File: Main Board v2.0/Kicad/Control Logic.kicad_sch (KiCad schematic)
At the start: 25 parts, among them J3 JTAG, J4 +3V3 Supply, J5 Conn_02x14_Counter_Clockwise, U7 XC95288XL-TQ144, U8 AP1117-33

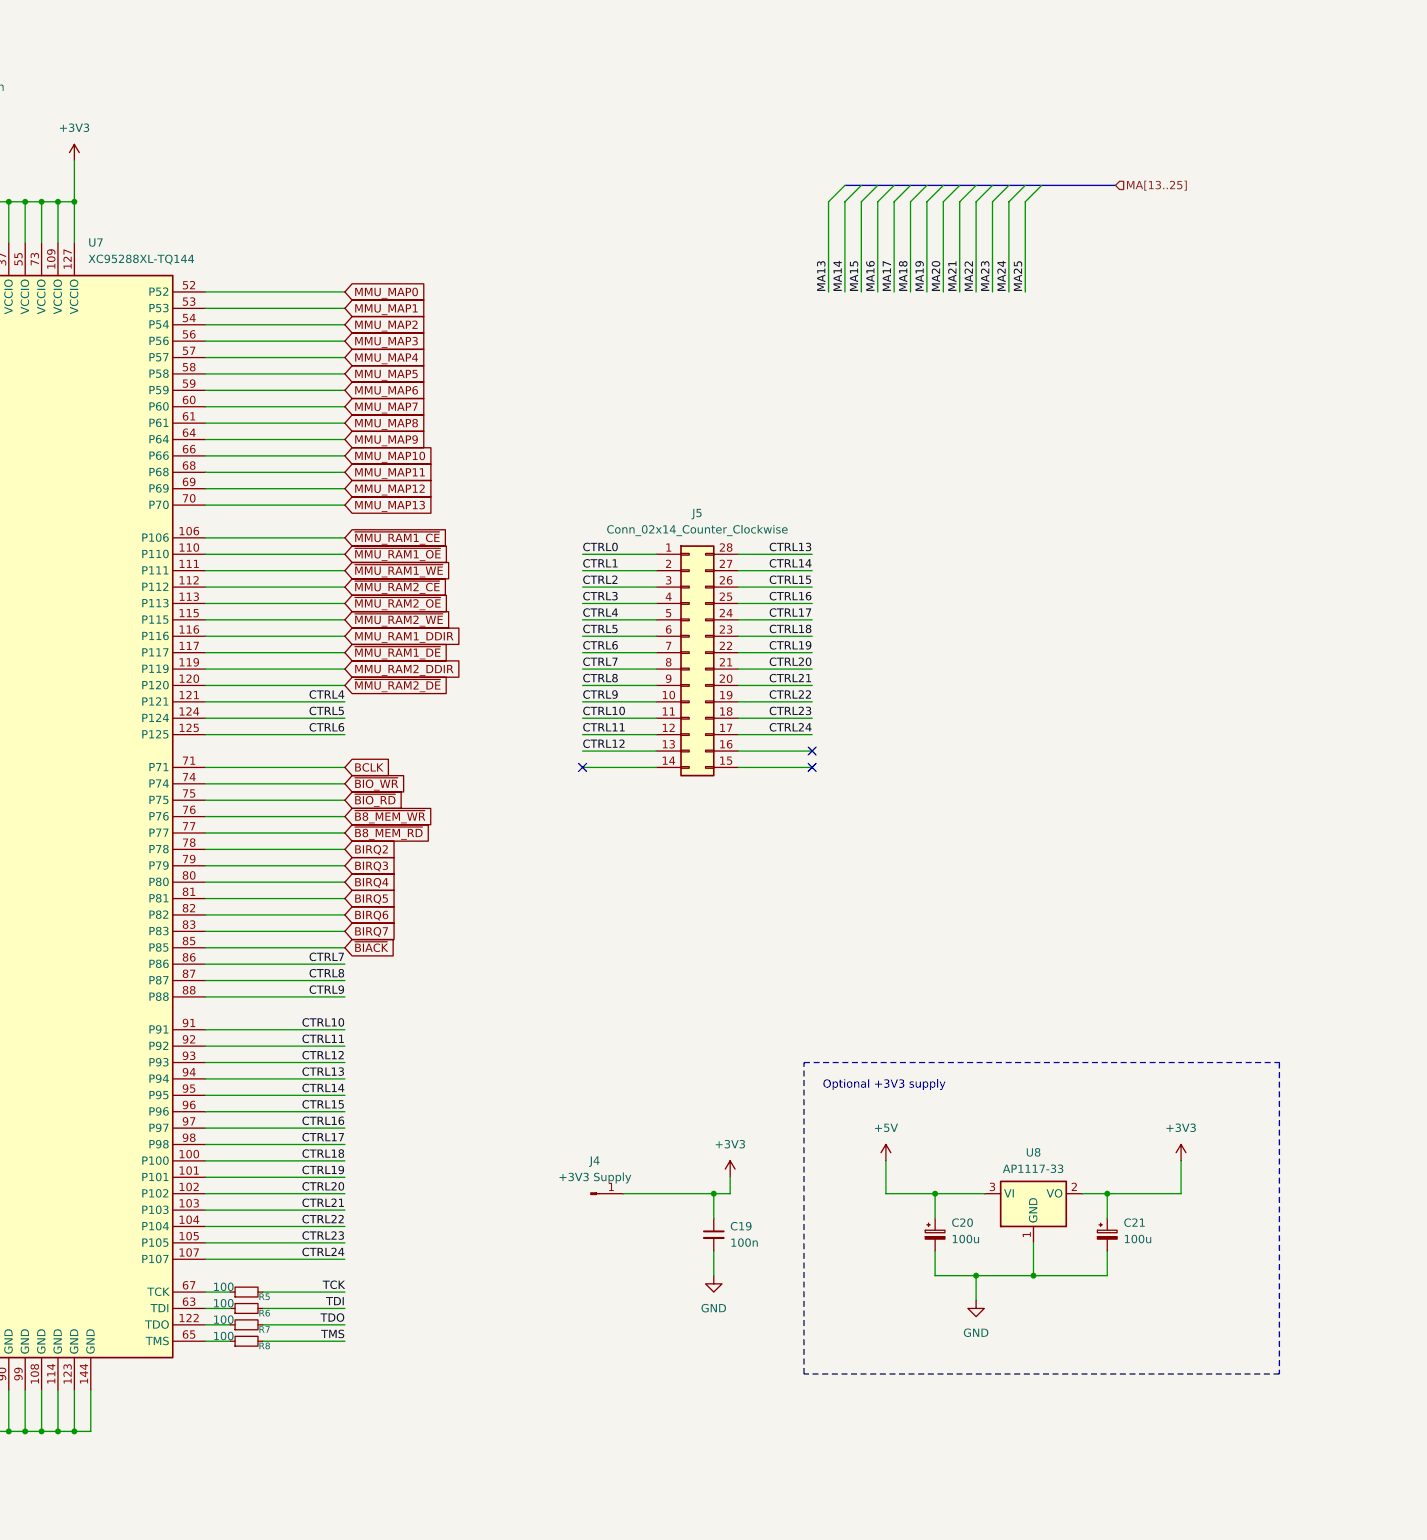
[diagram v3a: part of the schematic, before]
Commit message: schematic update
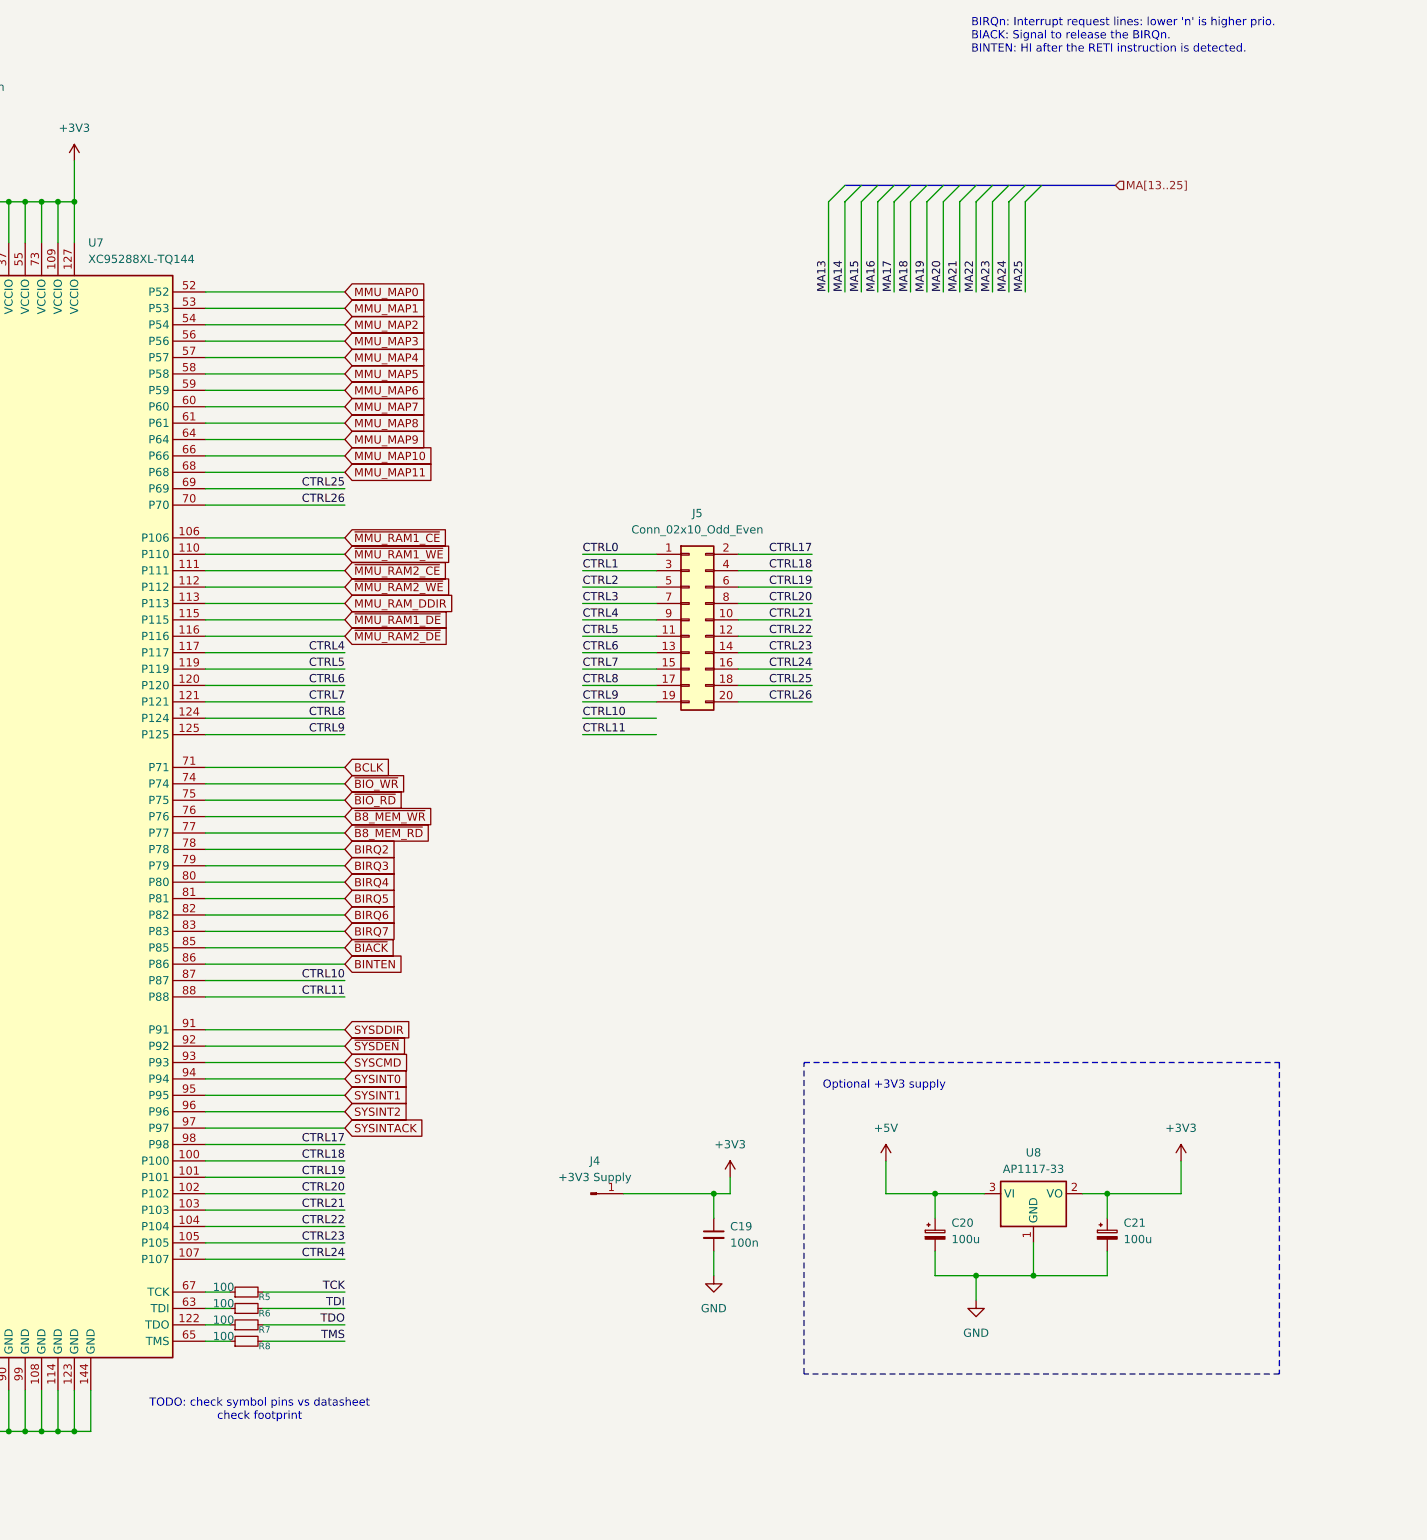
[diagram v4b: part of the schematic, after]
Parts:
- removed J5: Conn_02x14_Counter_Clockwise, Connector_PinSocket_2.54mm:PinSocket_2x14_P2.54mm_Vertical, symbol Connector_Generic:Conn_02x14_Counter_Clockwise
- added J5: Conn_02x10_Odd_Even, Connector_PinSocket_2.54mm:PinSocket_2x10_P2.54mm_Vertical, symbol Connector_Generic:Conn_02x10_Odd_Even
- C20, C21: footprint Capacitor_THT:CP_Radial_D10.0mm_P5.00mm -> Capacitor_THT:CP_Radial_D8.0mm_P3.80mm
- J3: footprint Connector_PinHeader_2.54mm:PinHeader_2x07_P2.54mm_Vertical -> Connector_IDC:IDC-Header_2x07_P2.54mm_Vertical
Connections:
- net MMU_RAM1_DDIR is gone; now on net ~{MMU_RAM2_DE}: U7.116 (P116)
- net MMU_RAM2_DDIR is gone; now on net CTRL5: U7.119 (P119)
- net ~{MMU_RAM1_OE} is gone; now on net ~{MMU_RAM1_WE}: U7.110 (P110)
- net CTRL0: now also J5.1 (Pin_1)
- net CTRL1: now also J5.3 (Pin_3)
- net CTRL10: now also U7.87 (P87); no longer U7.91 (P91)
- net CTRL11: now also U7.88 (P88); no longer U7.92 (P92)
- net CTRL17: now also J5.2 (Pin_2)
- net CTRL18: now also J5.4 (Pin_4)
- net CTRL19: now also J5.6 (Pin_6)
- net CTRL2: now also J5.5 (Pin_5)
- net CTRL20: now also J5.8 (Pin_8)
- net CTRL21: now also J5.10 (Pin_10)
- net CTRL22: now also J5.12 (Pin_12)
- net CTRL23: now also J5.14 (Pin_14)
- net CTRL24: now also J5.16 (Pin_16)
- net CTRL3: now also J5.7 (Pin_7)
- net CTRL4: now also U7.117 (P117), J5.9 (Pin_9); no longer U7.121 (P121)
- net CTRL5: now also J5.11 (Pin_11); no longer U7.124 (P124)
- net CTRL6: now also U7.120 (P120), J5.13 (Pin_13); no longer U7.125 (P125)
- net CTRL7: now also U7.121 (P121), J5.15 (Pin_15); no longer U7.86 (P86)
- net CTRL8: now also U7.124 (P124), J5.17 (Pin_17); no longer U7.87 (P87)
- net CTRL9: now also U7.125 (P125), J5.19 (Pin_19); no longer U7.88 (P88)
- net ~{MMU_RAM1_DE}: now also U7.115 (P115); no longer U7.117 (P117)
- net ~{MMU_RAM1_WE}: no longer U7.111 (P111)
- net ~{MMU_RAM2_CE}: now also U7.111 (P111); no longer U7.112 (P112)
- net ~{MMU_RAM2_DE}: no longer U7.120 (P120)
- net ~{MMU_RAM2_WE}: now also U7.112 (P112); no longer U7.115 (P115)
- net CTRL12 renamed SYSCMD
- net CTRL13 renamed SYSINT0
- net CTRL14 renamed SYSINT1
- net CTRL15 renamed SYSINT2
- net CTRL16 renamed SYSINTACK
- net MMU_MAP12 renamed CTRL25
- net CTRL25: now also J5.18 (Pin_18)
- net MMU_MAP13 renamed CTRL26
- net CTRL26: now also J5.20 (Pin_20)
- net ~{MMU_RAM2_OE} renamed MMU_RAM_DDIR
- new net BINTEN: U7.86 (P86)
- new net SYSDDIR: U7.91 (P91)
- new net ~{SYSDEN}: U7.92 (P92)
- no-connect marks 5 -> 2
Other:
- note added: "BIRQn: Interrupt request lines: lower 'n' is higher prio. BIACK: Signal to release the BIRQn. BINTEN: HI after the RETI instruction is detected."
- note added: "TODO: check symbol pins vs datasheet check footprint"

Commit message: schematic updates
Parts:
- removed J5: Conn_02x10_Odd_Even, Connector_PinSocket_2.54mm:PinSocket_2x10_P2.54mm_Vertical, symbol Connector_Generic:Conn_02x10_Odd_Even
- renumbered C12 to C10, C13 to C11, C14 to C12, C15 to C13, C16 to C14, C17 to C15, C18 to C16, C19 to C17, C20 to C18, C21 to C19, C9 to C7, C10 to C8, C11 to C9, J4 to J2, R5 to R28, R6 to R29, R7 to R30, R8 to R31, R2 to R32, R3 to R33, R4 to R34
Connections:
- net CTRL10 is gone; now on net ~{BIACK}: U7.87 (P87)
- net CTRL11 is gone; now on net BINTEN: U7.88 (P88)
- net BINTEN: no longer U7.86 (P86)
- net BIRQ2: now also U7.80 (P80); no longer U7.78 (P78)
- net BIRQ3: now also U7.81 (P81); no longer U7.79 (P79)
- net BIRQ4: now also U7.82 (P82); no longer U7.80 (P80)
- net BIRQ5: now also U7.83 (P83); no longer U7.81 (P81)
- net BIRQ6: now also U7.85 (P85); no longer U7.82 (P82)
- net BIRQ7: now also U7.86 (P86); no longer U7.83 (P83)
- net ~{BIACK}: no longer U7.85 (P85)
- net CTRL0 renamed BC11
- net CTRL1 renamed BC12
- net CTRL17 renamed BINTACK0
- net CTRL18 renamed BINTACK1
- net CTRL19 renamed BINTACK2
- net CTRL2 renamed BC13
- net CTRL20 renamed BINTACK3
- net CTRL21 renamed BINTACK4
- net CTRL22 renamed BINTACK5
- net CTRL23 renamed BINTACK6
- net CTRL24 renamed BINTACK7
- net CTRL25 renamed BC1
- net CTRL26 renamed BC6
- net CTRL3 renamed BC14
- net CTRL4 renamed BA1
- net CTRL5 renamed BB4
- net CTRL6 renamed BC15
- net CTRL7 renamed BC16
- net CTRL8 renamed BC17
- net CTRL9 renamed BC18
- new net BIRQ0: U7.78 (P78)
- new net BIRQ1: U7.79 (P79)
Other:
- note removed: "TODO: check symbol pins vs datasheet check footprint"

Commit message: board update
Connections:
- net BC6 is gone; now on net ~{CPU_RST}: U7.70 (P70)
- net MA25 is gone; now on net ~{CPU_INT}: U7.131 (P131)
- net MMU_MAP11 is gone; now on net D7: U7.68 (P68)
- net A0: now also U7.26 (P26); no longer U7.16 (P16)
- net A1: now also U7.27 (P27); no longer U7.17 (P17)
- net A10: now also U7.43 (P43); no longer U7.27 (P27)
- net A11: now also U7.44 (P44); no longer U7.28 (P28)
- net A12: now also U7.9 (P9); no longer U7.30 (I/O/GCK1)
- net A13: now also U7.10 (P10); no longer U7.31 (P31)
- net A14: now also U7.11 (P11); no longer U7.35 (P35)
- net A15: now also U7.12 (P12); no longer U7.2 (I/O/GTS3)
- net A2: now also U7.28 (P28); no longer U7.19 (P19)
- net A3: now also U7.30 (I/O/GCK1); no longer U7.20 (P20)
- net A4: now also U7.31 (P31); no longer U7.21 (P21)
- net A5: now also U7.35 (P35); no longer U7.22 (P22)
- net A6: now also U7.38 (I/O/GCK3); no longer U7.23 (P23)
- net A7: now also U7.39 (P39); no longer U7.24 (P24)
- net A8: now also U7.40 (P40); no longer U7.25 (P25)
- net A9: now also U7.41 (P41); no longer U7.26 (P26)
- net BA1: now also U7.69 (P69); no longer U7.117 (P117)
- net BB4: now also U7.71 (P71); no longer U7.119 (P119)
- net BC1: now also U7.24 (P24); no longer U7.69 (P69)
- net BC11: now also U7.132 (P132); no longer U7.137 (P137)
- net BC12: now also U7.133 (P133); no longer U7.138 (P138)
- net BC13: now also U7.134 (P134); no longer U7.139 (P139)
- net BC14: now also U7.135 (P135); no longer U7.140 (P140)
- net BC15: now also U7.136 (P136); no longer U7.120 (P120)
- net BC16: now also U7.137 (P137); no longer U7.121 (P121)
- net BC17: now also U7.138 (P138); no longer U7.124 (P124)
- net BC18: now also U7.139 (P139); no longer U7.125 (P125)
- net BCLK: now also U7.83 (P83); no longer U7.71 (P71)
- net BINTACK0: now also U7.16 (P16); no longer U7.98 (P98)
- net BINTACK1: now also U7.17 (P17); no longer U7.100 (P100)
- net BINTACK2: now also U7.2 (I/O/GTS3); no longer U7.101 (P101)
- net BINTACK3: now also U7.3 (I/O/GTS4); no longer U7.102 (P102)
- net BINTACK4: now also U7.4 (P4); no longer U7.103 (P103)
- net BINTACK5: now also U7.5 (I/O/GTS1); no longer U7.104 (P104)
- net BINTACK6: now also U7.6 (I/O/GTS2); no longer U7.105 (P105)
- net BINTACK7: now also U7.7 (P7); no longer U7.107 (P107)
- net BINTEN: now also U7.79 (P79); no longer U7.88 (P88)
- net BIRQ0: now also U7.32 (I/O/GCK2); no longer U7.78 (P78)
- net BIRQ1: now also U7.33 (P33); no longer U7.79 (P79)
- net BIRQ2: now also U7.34 (P34); no longer U7.80 (P80)
- net BIRQ3: now also U7.140 (P140); no longer U7.81 (P81)
- net BIRQ4: now also U7.88 (P88); no longer U7.82 (P82)
- net BIRQ5: now also U7.87 (P87); no longer U7.83 (P83)
- net BIRQ6: now also U7.86 (P86); no longer U7.85 (P85)
- net BIRQ7: now also U7.85 (P85); no longer U7.86 (P86)
- net CLK20: now also U7.13 (P13); no longer U7.32 (I/O/GCK2)
- net D0: now also U7.57 (P57); no longer U7.3 (I/O/GTS4)
- net D1: now also U7.58 (P58); no longer U7.4 (P4)
- net D2: now also U7.59 (P59); no longer U7.5 (I/O/GTS1)
- net D3: now also U7.60 (P60); no longer U7.6 (I/O/GTS2)
- net D4: now also U7.61 (P61); no longer U7.7 (P7)
- net D5: now also U7.64 (P64); no longer U7.9 (P9)
- net D6: now also U7.66 (P66); no longer U7.10 (P10)
- net D7: no longer U7.11 (P11)
- net MA13: now also U7.46 (P46); no longer U7.44 (P44)
- net MA14: now also U7.48 (P48); no longer U7.45 (P45)
- net MA15: now also U7.49 (P49); no longer U7.46 (P46)
- net MA16: now also U7.50 (P50); no longer U7.48 (P48)
- net MA17: now also U7.51 (P51); no longer U7.49 (P49)
- net MA18: now also U7.52 (P52); no longer U7.50 (P50)
- net MA19: now also U7.53 (P53); no longer U7.51 (P51)
- net MA20: now also U7.19 (P19); no longer U7.118 (P118)
- net MA21: now also U7.20 (P20); no longer U7.126 (P126)
- net MA22: now also U7.21 (P21); no longer U7.128 (P128)
- net MA23: now also U7.22 (P22); no longer U7.129 (P129)
- net MA24: now also U7.23 (P23); no longer U7.130 (P130)
- net MMU_MAP0: now also U7.95 (P95); no longer U7.52 (P52)
- net MMU_MAP1: now also U7.96 (P96); no longer U7.53 (P53)
- net MMU_MAP10: now also U7.107 (P107); no longer U7.66 (P66)
- net MMU_MAP2: now also U7.97 (P97); no longer U7.54 (P54)
- net MMU_MAP3: now also U7.98 (P98); no longer U7.56 (P56)
- net MMU_MAP4: now also U7.100 (P100); no longer U7.57 (P57)
- net MMU_MAP5: now also U7.101 (P101); no longer U7.58 (P58)
- net MMU_MAP6: now also U7.102 (P102); no longer U7.59 (P59)
- net MMU_MAP7: now also U7.103 (P103); no longer U7.60 (P60)
- net MMU_MAP8: now also U7.104 (P104); no longer U7.61 (P61)
- net MMU_MAP9: now also U7.105 (P105); no longer U7.64 (P64)
- net MMU_MP_EXE: now also U7.115 (P115); no longer U7.134 (P134)
- net MMU_MP_RD: now also U7.112 (P112); no longer U7.132 (P132)
- net MMU_MP_WR: now also U7.113 (P113); no longer U7.133 (P133)
- net MMU_RAM_DDIR: now also U7.92 (P92); no longer U7.113 (P113)
- net SYSCMD: now also U7.124 (P124); no longer U7.93 (P93)
- net SYSDDIR: now also U7.120 (P120); no longer U7.91 (P91)
- net SYSINT0: now also U7.126 (P126); no longer U7.94 (P94)
- net SYSINT1: now also U7.128 (P128); no longer U7.95 (P95)
- net SYSINT2: now also U7.129 (P129); no longer U7.96 (P96)
- net SYSINTACK: now also U7.125 (P125); no longer U7.97 (P97)
- net ~{B8_MEM_RD}: now also U7.75 (P75); no longer U7.77 (P77)
- net ~{B8_MEM_WR}: now also U7.74 (P74); no longer U7.76 (P76)
- net ~{BIACK}: now also U7.78 (P78); no longer U7.87 (P87)
- net ~{BIO_RD}: now also U7.77 (P77); no longer U7.75 (P75)
- net ~{BIO_WR}: now also U7.76 (P76); no longer U7.74 (P74)
- net ~{CPU_BUSACK}: now also U7.81 (P81); no longer U7.43 (P43)
- net ~{CPU_BUSRQ}: now also U7.80 (P80); no longer U7.41 (P41)
- net ~{CPU_HALT}: now also U7.119 (P119); no longer U7.33 (P33)
- net ~{CPU_INT}: no longer U7.14 (P14)
- net ~{CPU_IORQ}: now also U7.14 (P14); no longer U7.40 (P40)
- net ~{CPU_M1}: now also U7.54 (P54); no longer U7.15 (P15)
- net ~{CPU_MREQ}: now also U7.15 (P15); no longer U7.39 (P39)
- net ~{CPU_NMI}: now also U7.130 (P130); no longer U7.13 (P13)
- net ~{CPU_RD}: now also U7.142 (P142); no longer U7.34 (P34)
- net ~{CPU_RFSH}: now also U7.82 (P82); no longer U7.142 (P142)
- net ~{CPU_RST}: no longer U7.12 (P12)
- net ~{CPU_WAIT}: now also U7.56 (P56); no longer U7.143 (I/O/GSR)
- net ~{CPU_WR}: now also U7.143 (I/O/GSR); no longer U7.38 (I/O/GCK3)
- net ~{MMU_RAM1_CE}: now also U7.110 (P110); no longer U7.106 (P106)
- net ~{MMU_RAM1_DE}: now also U7.93 (P93); no longer U7.115 (P115)
- net ~{MMU_RAM1_WE}: now also U7.111 (P111); no longer U7.110 (P110)
- net ~{MMU_RAM2_CE}: now also U7.106 (P106); no longer U7.111 (P111)
- net ~{MMU_RAM2_DE}: now also U7.94 (P94); no longer U7.116 (P116)
- net ~{MMU_RAM2_WE}: now also U7.91 (P91); no longer U7.112 (P112)
- net ~{RAM_CE}: now also U7.117 (P117); no longer U7.136 (P136)
- net ~{ROM_CE}: now also U7.116 (P116); no longer U7.135 (P135)
- net ~{SYSDEN}: now also U7.121 (P121); no longer U7.92 (P92)
- new net BC2: U7.25 (P25)
- new net BC3: U7.118 (P118)
- new net MA12: U7.45 (P45)

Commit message: board update
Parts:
- removed R28, R29, R30, R31: 100, Resistor_SMD:R_0603_1608Metric_Pad0.98x0.95mm_HandSolder, symbol Device:R_Small
- C10, C11, C12, C13, C14, C15, C16, C17, C7, C8, C9, R32, R33, R34: KiLib_Generator (none) -> SMD_2terminal_chip_molded
- C18, C19: KiLib_Generator (none) -> capacitor/THT/other
- J2, J3: KiLib_Generator (none) -> connector/pin_header_socket
- U7: KiLib_Generator (none) -> package/gullwing
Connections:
- net BA1 is gone; now on net ~{CPU_WAIT}: U7.69 (P69)
- net BB4 is gone; now on net ~{CPU_RST}: U7.71 (P71)
- net A0: now also U7.28 (P28); no longer U7.26 (P26)
- net A1: now also U7.31 (P31); no longer U7.27 (P27)
- net A12: now also U7.136 (P136); no longer U7.9 (P9)
- net A13: now also U7.137 (P137); no longer U7.10 (P10)
- net A14: now also U7.138 (P138); no longer U7.11 (P11)
- net A15: now also U7.139 (P139); no longer U7.12 (P12)
- net A2: now also U7.32 (I/O/GCK2); no longer U7.28 (P28)
- net A3: now also U7.33 (P33); no longer U7.30 (I/O/GCK1)
- net A4: now also U7.34 (P34); no longer U7.31 (P31)
- net BC1: now also U7.27 (P27); no longer U7.24 (P24)
- net BC11: now also U7.16 (P16); no longer U7.132 (P132)
- net BC12: now also U7.15 (P15); no longer U7.133 (P133)
- net BC13: now also U7.14 (P14); no longer U7.134 (P134)
- net BC14: now also U7.13 (P13); no longer U7.135 (P135)
- net BC15: now also U7.12 (P12); no longer U7.136 (P136)
- net BC16: now also U7.11 (P11); no longer U7.137 (P137)
- net BC17: now also U7.10 (P10); no longer U7.138 (P138)
- net BC18: now also U7.9 (P9); no longer U7.139 (P139)
- net BC2: now also U7.26 (P26); no longer U7.25 (P25)
- net BC3: now also U7.25 (P25); no longer U7.118 (P118)
- net BINTACK0: now also U7.118 (P118); no longer U7.16 (P16)
- net BINTACK1: now also U7.132 (P132); no longer U7.17 (P17)
- net BINTACK2: now also U7.85 (P85); no longer U7.2 (I/O/GTS3)
- net BINTACK3: now also U7.86 (P86); no longer U7.3 (I/O/GTS4)
- net BINTACK4: now also U7.87 (P87); no longer U7.4 (P4)
- net BINTACK5: now also U7.7 (P7); no longer U7.5 (I/O/GTS1)
- net BINTACK6: now also U7.5 (I/O/GTS1); no longer U7.6 (I/O/GTS2)
- net BINTACK7: now also U7.3 (I/O/GTS4); no longer U7.7 (P7)
- net BIRQ0: now also U7.133 (P133); no longer U7.32 (I/O/GCK2)
- net BIRQ1: now also U7.134 (P134); no longer U7.33 (P33)
- net BIRQ2: now also U7.135 (P135); no longer U7.34 (P34)
- net BIRQ5: now also U7.6 (I/O/GTS2); no longer U7.87 (P87)
- net BIRQ6: now also U7.4 (P4); no longer U7.86 (P86)
- net BIRQ7: now also U7.2 (I/O/GTS3); no longer U7.85 (P85)
- net CLK20: now also U7.30 (I/O/GCK1); no longer U7.13 (P13)
- net MA20: now also U7.54 (P54); no longer U7.19 (P19)
- net MA21: now also U7.56 (P56); no longer U7.20 (P20)
- net MA22: now also U7.20 (P20); no longer U7.21 (P21)
- net MA23: now also U7.21 (P21); no longer U7.22 (P22)
- net MA24: now also U7.22 (P22); no longer U7.23 (P23)
- net TCK: now also U7.67 (TCK)
- net TDI: now also U7.63 (TDI)
- net TDO: now also U7.122 (TDO)
- net TMS: now also U7.65 (TMS)
- net ~{CPU_IORQ}: now also U7.142 (P142); no longer U7.14 (P14)
- net ~{CPU_M1}: now also U7.70 (P70); no longer U7.54 (P54)
- net ~{CPU_MREQ}: now also U7.143 (I/O/GSR); no longer U7.15 (P15)
- net ~{CPU_RD}: now also U7.19 (P19); no longer U7.142 (P142)
- net ~{CPU_RST}: no longer U7.70 (P70)
- net ~{CPU_WAIT}: no longer U7.56 (P56)
- net ~{CPU_WR}: now also U7.17 (P17); no longer U7.143 (I/O/GSR)
- net ~{RAM_CE}: now also U7.116 (P116); no longer U7.117 (P117)
- net ~{ROM_CE}: now also U7.117 (P117); no longer U7.116 (P116)
- new net BC4: U7.24 (P24)
- new net BC5: U7.23 (P23)
